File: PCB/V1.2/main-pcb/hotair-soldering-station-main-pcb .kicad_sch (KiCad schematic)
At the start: 140 parts, among them J1 230VAC_IN, J10 T12_power (NS-25 r2,54), J11 LCD_CON2 (JST r.2.0), J12 LCD_CON1 (JST r.2.0), J13 ICP (goldpin r2,54), J14 Unused_GPIO, J2 FRONT_PANEL (IDC r. 2,54), J3 EARTH_GND, J4 24V_IN (NS-25 r2,54), J5 PSUPPLY (PWZ-02S r.3,96), J6 HOTAIR_FAN (JST r,2,54), J7 HOTAIR_MEAS (JST r.2,5), J8 HOTAIR_HEATER (PWZ-02S r.3,96), J9 WEP (r.2,54), Q1 BC817, Q10 RFP15P05, Q11 BC817, Q12 BC817, Q13 BC817, Q14 BC807, Q15 RFP15P05, Q2 BC807, Q3 BC817, Q4 RFP15P05, Q5 BC817, Q6 BT139-600, Q7 BC817, Q8 BC807, Q9 BC817, U1 MOC3041M, U2 MAX31855KASA, U3 MP1584-Step-Down, U4 AP1117-ADJ, U5 LM741, U6 AD8606, U8 STM32F103C6Tx

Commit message: Add production files
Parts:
- C12, C6, C8, C9: value (none) -> 100n; footprint (none) -> Capacitors:0805
- C13, C18, C19: value (none) -> 10u; footprint (none) -> Capacitors:0805
- C20: value (none) -> 1u; footprint (none) -> Capacitors:0805
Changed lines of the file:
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@@
       (effects (font (size 0.889 0.889)) (justify left))
     )
-    (property "Value" "" (id 1) (at 479.425 158.115 0)
-      (effects (font (size 0.889 0.889)) (justify left))
-    )
-    (property "Footprint" "" (id 2) (at 479.7552 163.83 0)
+    (property "Value" "100n" (id 1) (at 479.425 158.115 0)
+      (effects (font (size 0.889 0.889)) (justify left))
+    )
+    (property "Footprint" "Capacitors:0805" (id 2) (at 479.7552 163.83 0)
       (effects (font (size 1.27 1.27)) hide)
     )
@@
       (effects (font (size 0.889 0.889)) (justify left))
     )
-    (property "Value" "" (id 1) (at 484.505 158.115 0)
-      (effects (font (size 0.889 0.889)) (justify left))
-    )
-    (property "Footprint" "" (id 2) (at 484.8352 163.83 0)
+    (property "Value" "100n" (id 1) (at 484.505 158.115 0)
+      (effects (font (size 0.889 0.889)) (justify left))
+    )
+    (property "Footprint" "Capacitors:0805" (id 2) (at 484.8352 163.83 0)
       (effects (font (size 1.27 1.27)) hide)
     )
@@
       (effects (font (size 0.889 0.889)) (justify left))
     )
-    (property "Value" "" (id 1) (at 489.585 158.115 0)
-      (effects (font (size 0.889 0.889)) (justify left))
-    )
-    (property "Footprint" "" (id 2) (at 489.9152 163.83 0)
+    (property "Value" "100n" (id 1) (at 489.585 158.115 0)
+      (effects (font (size 0.889 0.889)) (justify left))
+    )
+    (property "Footprint" "Capacitors:0805" (id 2) (at 489.9152 163.83 0)
       (effects (font (size 1.27 1.27)) hide)
     )
@@
       (effects (font (size 0.889 0.889)) (justify left))
     )
-    (property "Value" "" (id 1) (at 495.3 158.115 0)
-      (effects (font (size 0.889 0.889)) (justify left))
-    )
-    (property "Footprint" "" (id 2) (at 495.6302 163.83 0)
+    (property "Value" "100n" (id 1) (at 495.3 158.115 0)
+      (effects (font (size 0.889 0.889)) (justify left))
+    )
+    (property "Footprint" "Capacitors:0805" (id 2) (at 495.6302 163.83 0)
       (effects (font (size 1.27 1.27)) hide)
     )
@@
       (effects (font (size 0.889 0.889)) (justify left))
     )
-    (property "Value" "" (id 1) (at 501.65 158.115 0)
-      (effects (font (size 0.889 0.889)) (justify left))
-    )
-    (property "Footprint" "" (id 2) (at 501.9802 163.83 0)
+    (property "Value" "10u" (id 1) (at 501.65 158.115 0)
+      (effects (font (size 0.889 0.889)) (justify left))
+    )
+    (property "Footprint" "Capacitors:0805" (id 2) (at 501.9802 163.83 0)
       (effects (font (size 1.27 1.27)) hide)
     )
@@
       (effects (font (size 0.889 0.889)) (justify left))
     )
-    (property "Value" "" (id 1) (at 507.365 158.115 0)
-      (effects (font (size 0.889 0.889)) (justify left))
-    )
-    (property "Footprint" "" (id 2) (at 507.6952 163.83 0)
+    (property "Value" "10u" (id 1) (at 507.365 158.115 0)
+      (effects (font (size 0.889 0.889)) (justify left))
+    )
+    (property "Footprint" "Capacitors:0805" (id 2) (at 507.6952 163.83 0)
       (effects (font (size 1.27 1.27)) hide)
     )
@@
       (effects (font (size 0.889 0.889)) (justify left))
     )
-    (property "Value" "" (id 1) (at 513.08 158.115 0)
-      (effects (font (size 0.889 0.889)) (justify left))
-    )
-    (property "Footprint" "" (id 2) (at 513.4102 163.83 0)
+    (property "Value" "10u" (id 1) (at 513.08 158.115 0)
+      (effects (font (size 0.889 0.889)) (justify left))
+    )
+    (property "Footprint" "Capacitors:0805" (id 2) (at 513.4102 163.83 0)
       (effects (font (size 1.27 1.27)) hide)
     )
@@
       (effects (font (size 0.889 0.889)) (justify left))
     )
-    (property "Value" "" (id 1) (at 518.795 158.115 0)
-      (effects (font (size 0.889 0.889)) (justify left))
-    )
-    (property "Footprint" "" (id 2) (at 519.1252 163.83 0)
+    (property "Value" "1u" (id 1) (at 518.795 158.115 0)
+      (effects (font (size 0.889 0.889)) (justify left))
+    )
+    (property "Footprint" "Capacitors:0805" (id 2) (at 519.1252 163.83 0)
       (effects (font (size 1.27 1.27)) hide)
     )
@@
   (symbol (lib_id "Device:R") (at 125.73 347.345 0) (mirror x) (unit 1)
     (in_bom yes) (on_board yes)
-    (property "Reference" "R32" (id 0) (at 128.27 350.52 90)
-      (effects (font (size 1.27 1.27)) (justify right))
-    )
-    (property "Value" "10k" (id 1) (at 128.27 347.345 90)
-      (effects (font (size 1.27 1.27)) (justify right))
-    )
+    (property "Reference" "R32" (id 0) (at 130.81 345.44 0)
+      (effects (font (size 1.27 1.27)) (justify right))
+    )
+    (property "Value" "10k" (id 1) (at 130.81 347.98 0)
+      (effects (font (size 1.27 1.27)) (justify right))
+    )

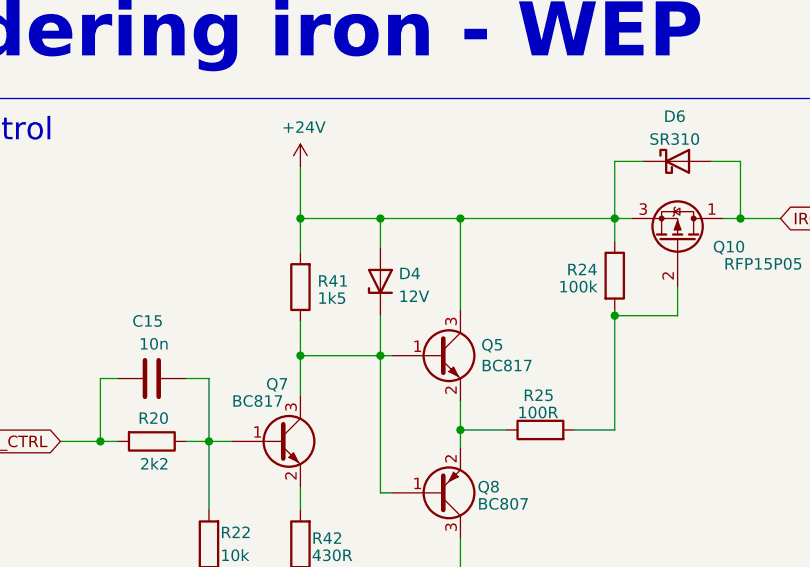
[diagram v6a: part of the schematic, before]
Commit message: Zener diode footprint and orientation change
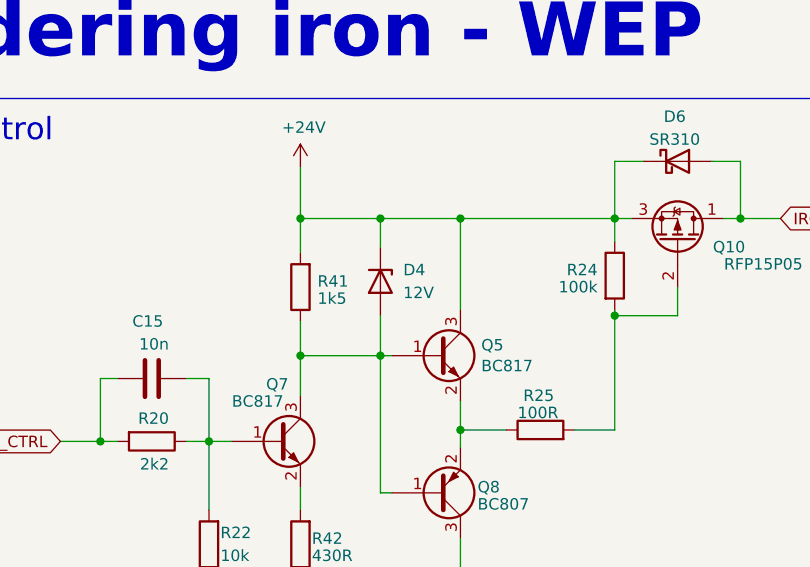
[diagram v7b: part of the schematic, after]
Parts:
- D4, D9: footprint Diode_SMD:D_0805_2012Metric -> Diode_SMD:D_MiniMELF
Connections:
- net +24V: now also D4.1 (K); no longer D4.2 (A)
- net at Q5.1 (B), Q7.3 (C), Q8.1 (B)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: now also D4.2 (A); no longer D4.1 (K)
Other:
- moved on the sheet: D4
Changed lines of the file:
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@@
     (pin "2")
     (pin "3")
+  )
+  (symbol (lib_id "SparkFun-IC-Amplifiers:LM358") (at 383.54 247.65 0) (unit 2)
+    (in_bom yes) (on_board yes)
+    (property "Reference" "U6" (id 0) (at 383.54 238.6584 0)
+      (effects (font (size 1.143 1.143)))
+    )
+    (property "Value" "AD8606" (id 1) (at 383.54 240.792 0)
+      (effects (font (size 1.143 1.143)))
+    )
+    (property "Footprint" "Package_SO:SO-8_3.9x4.9mm_P1.27mm" (id 2) (at 383.54 238.76 0)
+      (effects (font (size 0.508 0.508)) hide)
+    )
+    (property "Datasheet" "" (id 3) (at 383.54 247.65 0)
+      (effects (font (size 1.27 1.27)) hide)
+    )
+    (property "Pole4" "IC-09172" (id 4) (at 383.54 240.5126 0)
+      (effects (font (size 1.524 1.524)) hide)
+    )
     (pin "5")
     (pin "6")
     (pin "7")
-    (pin "4")
-    (pin "8")
-  )
-  (symbol (lib_id "SparkFun-IC-Amplifiers:LM358") (at 383.54 247.65 0) (unit 2)
-    (in_bom yes) (on_board yes)
-    (property "Reference" "U6" (id 0) (at 383.54 238.6584 0)
-      (effects (font (size 1.143 1.143)))
-    )
-    (property "Value" "AD8606" (id 1) (at 383.54 240.792 0)
-      (effects (font (size 1.143 1.143)))
-    )
-    (property "Footprint" "Package_SO:SO-8_3.9x4.9mm_P1.27mm" (id 2) (at 383.54 238.76 0)
-      (effects (font (size 0.508 0.508)) hide)
-    )
-    (property "Datasheet" "" (id 3) (at 383.54 247.65 0)
-      (effects (font (size 1.27 1.27)) hide)
-    )
-    (property "Pole4" "IC-09172" (id 4) (at 383.54 240.5126 0)
-      (effects (font (size 1.524 1.524)) hide)
-    )
-    (pin "1")
-    (pin "2")
-    (pin "3")
-    (pin "5")
-    (pin "6")
-    (pin "7")
-    (pin "4")
-    (pin "8")
   )
   (symbol (lib_id "SparkFun-IC-Amplifiers:LM358") (at 421.64 227.965 0) (unit 3)
@@
       (effects (font (size 1.524 1.524)) (justify left) hide)
     )
-    (pin "1")
-    (pin "2")
-    (pin "3")
-    (pin "5")
-    (pin "6")
-    (pin "7")
     (pin "4")
     (pin "8")
@@
       (effects (font (size 1.27 1.27)) (justify left))
     )
-    (property "Footprint" "Diode_SMD:D_0805_2012Metric" (id 2) (at 371.475 163.195 0)
+    (property "Footprint" "Diode_SMD:D_MiniMELF" (id 2) (at 371.475 163.195 0)
       (effects (font (size 1.27 1.27)) hide)
     )
@@
     (pin "2")
   )
-  (symbol (lib_id "Device:D_Zener") (at 232.41 161.29 90) (unit 1)
+  (symbol (lib_id "Device:D_Zener") (at 232.41 161.29 270) (unit 1)
     (in_bom yes) (on_board yes) (fields_autoplaced)
-    (property "Reference" "D4" (id 0) (at 234.442 160.4553 90)
-      (effects (font (size 1.27 1.27)) (justify right))
-    )
-    (property "Value" "12V" (id 1) (at 234.442 162.9922 90)
-      (effects (font (size 1.27 1.27)) (justify right))
-    )
-    (property "Footprint" "Diode_SMD:D_0805_2012Metric" (id 2) (at 232.41 161.29 0)
+    (property "Reference" "D4" (id 0) (at 234.95 160.0199 90)
+      (effects (font (size 1.27 1.27)) (justify left))
+    )
+    (property "Value" "12V" (id 1) (at 234.95 162.5599 90)
+      (effects (font (size 1.27 1.27)) (justify left))
+    )
+    (property "Footprint" "Diode_SMD:D_MiniMELF" (id 2) (at 232.41 161.29 0)
       (effects (font (size 1.27 1.27)) hide)
     )
@@
     )
     (path "/968dadfa-c257-41f0-b295-899c8d490abe"
-      (reference "D4") (unit 1) (value "12V") (footprint "Diode_SMD:D_0805_2012Metric")
+      (reference "D4") (unit 1) (value "12V") (footprint "Diode_SMD:D_MiniMELF")
     )
     (path "/00000000-0000-0000-0000-00005fbd8862"
@@
     )
     (path "/4a8ae321-5ad7-4607-8022-288a4577f606"
-      (reference "D9") (unit 1) (value "12V") (footprint "Diode_SMD:D_0805_2012Metric")
+      (reference "D9") (unit 1) (value "12V") (footprint "Diode_SMD:D_MiniMELF")
     )
     (path "/b781b47f-83df-4e75-ab30-24a3cb47eb1b"
